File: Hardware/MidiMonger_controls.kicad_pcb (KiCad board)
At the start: 2 copper layers, 40 x 110 mm, 31 parts, among them J10 Gate8_Out, J11 CV1_Out, J12 CV2_Out, J13 CV3_Out, J14 CV4_Out, J15 USB_B_Wurth, J16 MIDI_DIN, J2 Gate3_Out, J20 Conn_01x09_Female, J21 Conn_01x08_Female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

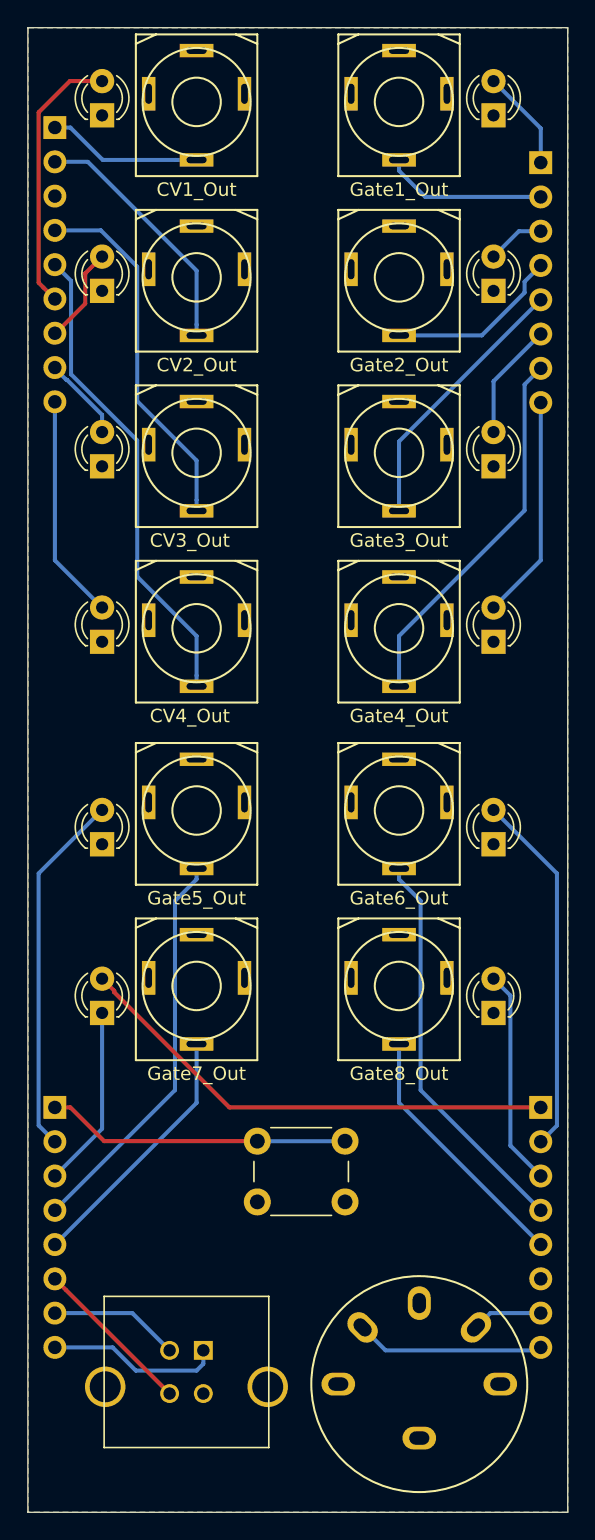
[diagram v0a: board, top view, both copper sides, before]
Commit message: Panel first draft with components
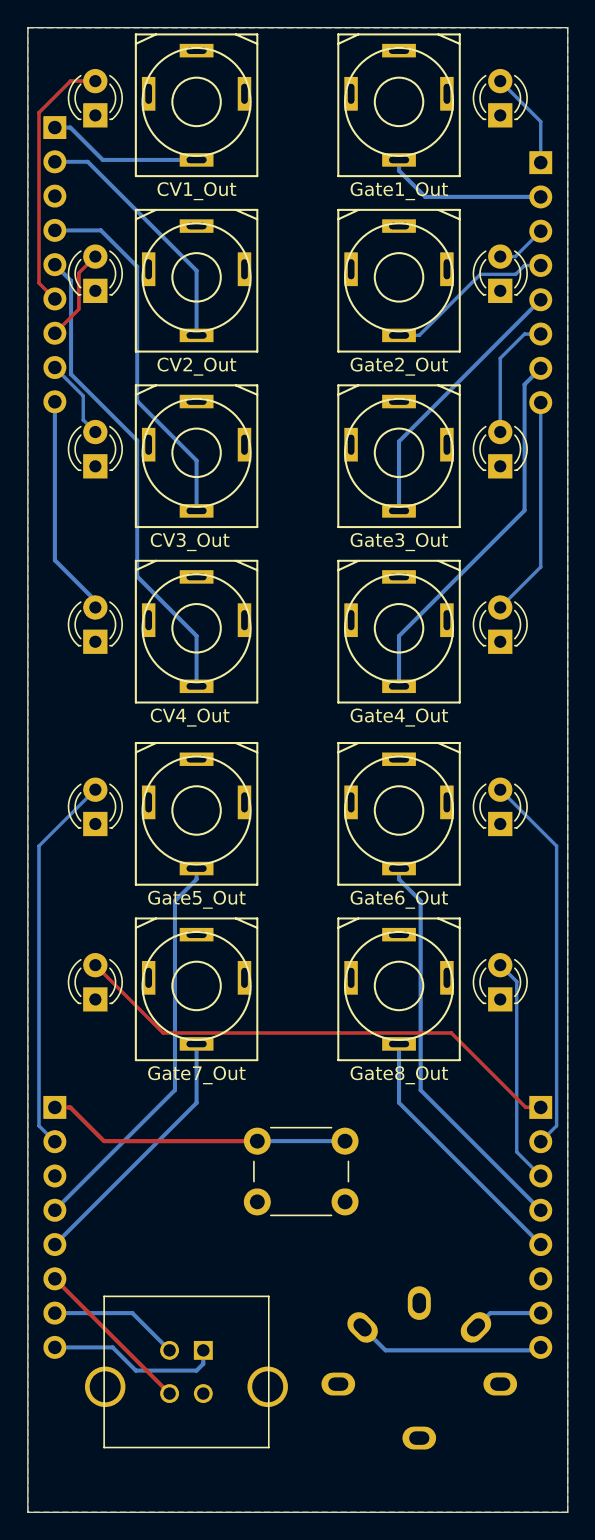
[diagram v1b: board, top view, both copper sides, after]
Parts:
- moved D10 1.58 mm to (131.0, 99.0)
- moved D9 1.58 mm to (101.0, 99.0)
- moved D11 1.12 mm to (101.0, 112.0)
- moved D12 1.12 mm to (131.0, 112.0)
- moved D1 0.50 mm to (131.0, 46.5)
- moved D2 0.50 mm to (131.0, 59.5)
- moved D3 0.50 mm to (131.0, 72.5)
- moved D4 0.50 mm to (131.0, 85.5)
- moved D5 0.50 mm to (101.0, 46.5)
- moved D6 0.50 mm to (101.0, 59.5)
- moved D7 0.50 mm to (101.0, 72.5)
- moved D8 0.50 mm to (101.0, 85.5)
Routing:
- net GND: track 13.5 -> 0.00 mm
- net GATE6_LED_OUT: track 27.0 -> 28.3 mm
- net GATE5_LED_OUT: track 27.0 -> 28.3 mm
- net GATE7_LED_OUT: track 36.5 -> 37.4 mm
- net GATE8_LED_OUT: track 16.1 -> 16.9 mm
- net CV1_LED_OUT: track 20.0 -> 19.4 mm
- net GATE2_LED_OUT: track 4.28 -> 3.78 mm

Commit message: First draft of PCBs completed and sent to JLC
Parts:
- moved J15 2.06 mm to (108.5, 140.0)
- moved SW1 2.02 mm to (112.8, 124.5)
- moved D10 2.00 mm to (131.0, 101.0)
- moved D11 2.00 mm to (101.0, 114.0)
- moved D12 2.00 mm to (131.0, 114.0)
- moved D9 2.00 mm to (101.0, 101.0)
- moved J10 2.00 mm to (123.5, 114.0)
- moved J7 2.00 mm to (108.5, 101.0)
- moved J8 2.00 mm to (123.5, 101.0)
- moved J9 2.00 mm to (108.5, 114.0)
- moved J16 1.00 mm to (125.0, 135.5)
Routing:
- net GATE6_LED_OUT: track 28.3 -> 26.2 mm
- net GATE5_LED_OUT: track 28.3 -> 26.2 mm
- net GATE8_OUT: track 19.2 -> 17.2 mm
- net GATE7_OUT: track 19.2 -> 17.2 mm
- net GATE6_OUT: track 29.7 -> 27.7 mm
- net GATE5_OUT: track 29.7 -> 27.7 mm
- net USB_DP: track 12.0 -> 13.8 mm
- net USB_VBUS: track 13.2 -> 14.2 mm
- net RESET_SWITCH: track 22.5 -> 23.4 mm
- net GATE7_LED_OUT: track 37.4 -> 36.5 mm
- net GATE2_OUT: track 12.6 -> 13.5 mm
- net GATE3_LED_OUT: track 9.21 -> 8.50 mm
- net CV4_LED_OUT: track 16.6 -> 17.2 mm
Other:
- net class Default: clearance 0.2 -> 0.25; trace_width 0.25 -> 0.4
- rule trace_clearance: 0.2 -> 0.25
- board text added: "CV1"
- board text added: "CV1-4LED"
- board text added: "CV2"
- board text added: "CV3"
- board text added: "DM"
- board text added: "G1"
- board text added: "G1L"
- board text added: "G2L"
- board text added: "G3L"
- board text added: "G4"
- board text added: "G4L"
- board text added: "G5"
- board text added: "G5L"
- board text added: "G6"
- board text added: "G6L"
- board text added: "G7"
- board text added: "G7L"
- board text added: "G8"
- board text added: "G8L"
- board text added: "GND"
- board text added: "MD"
- board text added: "MV"
- board text added: "Mountjoy Modular MIDI Monger Controls v1.0"
- board text added: "RES"
- board text added: "USB DP"
- board text added: "VBUS"

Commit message: Fixed grounding error with output jacks on controls board
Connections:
- J10 pad 2: GND -> Net-(J10-Pad2)
- J11 pad 2: GND -> Net-(J11-Pad2)
- J12 pad 2: GND -> Net-(J12-Pad2)
- J13 pad 2: GND -> Net-(J13-Pad2)
- J14 pad 2: GND -> Net-(J14-Pad2)
- J2 pad 2: GND -> Net-(J2-Pad2)
- J3 pad 2: GND -> Net-(J3-Pad2)
- J4 pad 2: GND -> Net-(J4-Pad2)
- J5 pad 2: GND -> Net-(J5-Pad2)
- J7 pad 2: GND -> Net-(J7-Pad2)
- J8 pad 2: GND -> Net-(J8-Pad2)
- J9 pad 2: GND -> Net-(J9-Pad2)
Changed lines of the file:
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@@
-(kicad_pcb (version 20171130) (host pcbnew "(5.1.4)-1")
+(kicad_pcb (version 20171130) (host pcbnew "(5.1.5)-3")
   (general
     (thickness 1.6)
@@
     (zones 0)
     (modules 31)
-    (nets 36)
+    (nets 49)
   )
   (page A4)
   (layers
-    (0 F.Cu signal hide)
-    (31 B.Cu signal hide)
+    (0 F.Cu signal)
+    (31 B.Cu signal)
     (32 B.Adhes user)
     (33 F.Adhes user)
@@
   (net 34 CV3_OUT)
   (net 35 CV4_OUT)
+  (net 36 "Net-(J2-Pad2)")
+  (net 37 "Net-(J3-Pad2)")
+  (net 38 "Net-(J4-Pad2)")
+  (net 39 "Net-(J5-Pad2)")
+  (net 40 "Net-(J7-Pad2)")
+  (net 41 "Net-(J8-Pad2)")
+  (net 42 "Net-(J9-Pad2)")
+  (net 43 "Net-(J10-Pad2)")
+  (net 44 "Net-(J11-Pad2)")
+  (net 45 "Net-(J12-Pad2)")
+  (net 46 "Net-(J13-Pad2)")
+  (net 47 "Net-(J14-Pad2)")
+  (net 48 "Net-(J15-Pad5)")
   (net_class Default "This is the default net class."
     (clearance 0.25)
@@
     (add_net MIDI_DATA)
     (add_net MIDI_VREF)
+    (add_net "Net-(J10-Pad2)")
+    (add_net "Net-(J11-Pad2)")
+    (add_net "Net-(J12-Pad2)")
+    (add_net "Net-(J13-Pad2)")
+    (add_net "Net-(J14-Pad2)")
+    (add_net "Net-(J15-Pad5)")
     (add_net "Net-(J16-Pad1)")
     (add_net "Net-(J16-Pad2)")
     (add_net "Net-(J16-Pad3)")
     (add_net "Net-(J16-Pad6)")
+    (add_net "Net-(J2-Pad2)")
+    (add_net "Net-(J3-Pad2)")
+    (add_net "Net-(J4-Pad2)")
+    (add_net "Net-(J5-Pad2)")
+    (add_net "Net-(J7-Pad2)")
+    (add_net "Net-(J8-Pad2)")
+    (add_net "Net-(J9-Pad2)")
     (add_net RESET_SWITCH)
     (add_net USB_DM)
     (add_net USB_DP)
     (add_net USB_VBUS)
+  )
+  (module Custom_Footprints:USB_B_Wurth (layer F.Cu)
+    (at 108.5 140)
+    (descr "USB B female connector, straight, rugged")
+    (tags "USB_B_MUSB_Straight female connector straight rugged MUSB D511")
+    (fp_text reference J15 (at -0.9 -5) (layer F.SilkS) hide
+      (effects (font (size 1 1) (thickness 0.15)))
+    )
+    (fp_text value USB_B_Wurth (at -0.9 8.7) (layer F.Fab)
+      (effects (font (size 1 1) (thickness 0.15)))
+    )
+    (fp_line (start 4.85 -4) (end 4.85 7.2) (layer F.SilkS) (width 0.12))
+    (fp_line (start -7.35 7.2) (end 4.85 7.2) (layer F.SilkS) (width 0.12))
+    (fp_line (start -7.35 -4) (end 4.85 -4) (layer F.SilkS) (width 0.12))
+    (fp_line (start -7.35 -4) (end -7.35 7.2) (layer F.SilkS) (width 0.12))
+    (fp_line (start -9 -4.3) (end 6.5 -4.3) (layer F.CrtYd) (width 0.05))
+    (fp_line (start 6.5 -4.3) (end 6.5 7.5) (layer F.CrtYd) (width 0.05))
+    (fp_line (start 6.5 7.5) (end -9 7.5) (layer F.CrtYd) (width 0.05))
+    (fp_line (start -9 7.5) (end -9 -4.3) (layer F.CrtYd) (width 0.05))
+    (pad 5 thru_hole circle (at 4.77 2.7) (size 3 3) (drill 2.3) (layers *.Cu *.Mask)
+      (net 48 "Net-(J15-Pad5)"))
+    (pad 4 thru_hole circle (at 0 3.2) (size 1.4 1.4) (drill 0.92) (layers *.Cu *.Mask)
+      (net 2 GND))
+    (pad 3 thru_hole circle (at -2.5 3.2) (size 1.4 1.4) (drill 0.92) (layers *.Cu *.Mask)
+      (net 26 USB_DP))
+    (pad 1 thru_hole rect (at 0 0) (size 1.4 1.4) (drill 0.92) (layers *.Cu *.Mask)
+      (net 27 USB_VBUS))
+    (pad "" thru_hole circle (at -7.27 2.7) (size 3 3) (drill 2.3) (layers *.Cu *.Mask))
+    (pad 2 thru_hole circle (at -2.5 0) (size 1.4 1.4) (drill 0.92) (layers *.Cu *.Mask)
+      (net 25 USB_DM))
   )
   (module Custom_Footprints:MIDI_DIN (layer F.Cu)
@@
     )
   )
-  (module Custom_Footprints:USB_B_Wurth (layer F.Cu)
-    (at 108.5 140)
-    (descr "USB B female connector, straight, rugged")
-    (tags "USB_B_MUSB_Straight female connector straight rugged MUSB D511")
-    (fp_text reference J15 (at -0.9 -5) (layer F.SilkS) hide
-      (effects (font (size 1 1) (thickness 0.15)))
-    )
-    (fp_text value USB_B_Wurth (at -0.9 8.7) (layer F.Fab)
-      (effects (font (size 1 1) (thickness 0.15)))
-    )
-    (fp_line (start 4.85 -4) (end 4.85 7.2) (layer F.SilkS) (width 0.12))
-    (fp_line (start -7.35 7.2) (end 4.85 7.2) (layer F.SilkS) (width 0.12))
-    (fp_line (start -7.35 -4) (end 4.85 -4) (layer F.SilkS) (width 0.12))
-    (fp_line (start -7.35 -4) (end -7.35 7.2) (layer F.SilkS) (width 0.12))
-    (fp_line (start -9 -4.3) (end 6.5 -4.3) (layer F.CrtYd) (width 0.05))
-    (fp_line (start 6.5 -4.3) (end 6.5 7.5) (layer F.CrtYd) (width 0.05))
-    (fp_line (start 6.5 7.5) (end -9 7.5) (layer F.CrtYd) (width 0.05))
-    (fp_line (start -9 7.5) (end -9 -4.3) (layer F.CrtYd) (width 0.05))
-    (pad "" thru_hole circle (at 4.77 2.7) (size 3 3) (drill 2.3) (layers *.Cu *.Mask))
-    (pad 4 thru_hole circle (at 0 3.2) (size 1.4 1.4) (drill 0.92) (layers *.Cu *.Mask)
-      (net 2 GND))
-    (pad 3 thru_hole circle (at -2.5 3.2) (size 1.4 1.4) (drill 0.92) (layers *.Cu *.Mask)
-      (net 26 USB_DP))
-    (pad 1 thru_hole rect (at 0 0) (size 1.4 1.4) (drill 0.92) (layers *.Cu *.Mask)
-      (net 27 USB_VBUS))
-    (pad "" thru_hole circle (at -7.27 2.7) (size 3 3) (drill 2.3) (layers *.Cu *.Mask))
-    (pad 2 thru_hole circle (at -2.5 0) (size 1.4 1.4) (drill 0.92) (layers *.Cu *.Mask)
-      (net 25 USB_DM))
-  )
   (module Custom_Footprints:Cliff_3.5mm_Stereo_Jack (layer F.Cu)
     (at 123.5 72.5)
@@
       (net 2 GND))
     (pad 2 thru_hole rect (at -3.55 -1.6 90) (size 2.5 1) (drill oval 1.5 0.5) (layers *.Cu *.Mask F.SilkS)
-      (net 2 GND))
+      (net 36 "Net-(J2-Pad2)"))
     (pad 3 thru_hole rect (at 0 3.3) (size 2.5 1) (drill oval 1.5 0.5) (layers *.Cu *.Mask F.SilkS)
       (net 23 GATE3_OUT))
@@
       (net 2 GND))
     (pad 2 thru_hole rect (at -3.55 -1.6 90) (size 2.5 1) (drill oval 1.5 0.5) (layers *.Cu *.Mask F.SilkS)
-      (net 2 GND))
+      (net 37 "Net-(J3-Pad2)"))
     (pad 3 thru_hole rect (at 0 3.3) (size 2.5 1) (drill oval 1.5 0.5) (layers *.Cu *.Mask F.SilkS)
       (net 24 GATE4_OUT))
@@
       (net 2 GND))
     (pad 2 thru_hole rect (at -3.55 -1.6 90) (size 2.5 1) (drill oval 1.5 0.5) (layers *.Cu *.Mask F.SilkS)
-      (net 2 GND))
+      (net 38 "Net-(J4-Pad2)"))
     (pad 3 thru_hole rect (at 0 3.3) (size 2.5 1) (drill oval 1.5 0.5) (layers *.Cu *.Mask F.SilkS)
       (net 21 GATE1_OUT))
@@
       (net 2 GND))
     (pad 2 thru_hole rect (at -3.55 -1.6 90) (size 2.5 1) (drill oval 1.5 0.5) (layers *.Cu *.Mask F.SilkS)
-      (net 2 GND))
+      (net 39 "Net-(J5-Pad2)"))
     (pad 3 thru_hole rect (at 0 3.3) (size 2.5 1) (drill oval 1.5 0.5) (layers *.Cu *.Mask F.SilkS)
       (net 22 GATE2_OUT))
@@
       (net 2 GND))
     (pad 2 thru_hole rect (at -3.55 -1.6 90) (size 2.5 1) (drill oval 1.5 0.5) (layers *.Cu *.Mask F.SilkS)
-      (net 2 GND))
+      (net 40 "Net-(J7-Pad2)"))
     (pad 3 thru_hole rect (at 0 3.3) (size 2.5 1) (drill oval 1.5 0.5) (layers *.Cu *.Mask F.SilkS)
       (net 20 GATE5_OUT))
@@
       (net 2 GND))
     (pad 2 thru_hole rect (at -3.55 -1.6 90) (size 2.5 1) (drill oval 1.5 0.5) (layers *.Cu *.Mask F.SilkS)
-      (net 2 GND))
+      (net 41 "Net-(J8-Pad2)"))
     (pad 3 thru_hole rect (at 0 3.3) (size 2.5 1) (drill oval 1.5 0.5) (layers *.Cu *.Mask F.SilkS)
       (net 19 GATE6_OUT))
@@
       (net 2 GND))
     (pad 2 thru_hole rect (at -3.55 -1.6 90) (size 2.5 1) (drill oval 1.5 0.5) (layers *.Cu *.Mask F.SilkS)
-      (net 2 GND))
+      (net 42 "Net-(J9-Pad2)"))
     (pad 3 thru_hole rect (at 0 3.3) (size 2.5 1) (drill oval 1.5 0.5) (layers *.Cu *.Mask F.SilkS)
       (net 18 GATE7_OUT))
@@
       (net 2 GND))
     (pad 2 thru_hole rect (at -3.55 -1.6 90) (size 2.5 1) (drill oval 1.5 0.5) (layers *.Cu *.Mask F.SilkS)
-      (net 2 GND))
+      (net 43 "Net-(J10-Pad2)"))
     (pad 3 thru_hole rect (at 0 3.3) (size 2.5 1) (drill oval 1.5 0.5) (layers *.Cu *.Mask F.SilkS)
       (net 17 GATE8_OUT))
@@
       (net 2 GND))
     (pad 2 thru_hole rect (at -3.55 -1.6 90) (size 2.5 1) (drill oval 1.5 0.5) (layers *.Cu *.Mask F.SilkS)
-      (net 2 GND))
+      (net 44 "Net-(J11-Pad2)"))
     (pad 3 thru_hole rect (at 0 3.3) (size 2.5 1) (drill oval 1.5 0.5) (layers *.Cu *.Mask F.SilkS)
       (net 32 CV1_OUT))
@@
       (net 2 GND))
     (pad 2 thru_hole rect (at -3.55 -1.6 90) (size 2.5 1) (drill oval 1.5 0.5) (layers *.Cu *.Mask F.SilkS)
-      (net 2 GND))
+      (net 45 "Net-(J12-Pad2)"))
     (pad 3 thru_hole rect (at 0 3.3) (size 2.5 1) (drill oval 1.5 0.5) (layers *.Cu *.Mask F.SilkS)
       (net 33 CV2_OUT))
@@
       (net 2 GND))
     (pad 2 thru_hole rect (at -3.55 -1.6 90) (size 2.5 1) (drill oval 1.5 0.5) (layers *.Cu *.Mask F.SilkS)
-      (net 2 GND))
+      (net 46 "Net-(J13-Pad2)"))
     (pad 3 thru_hole rect (at 0 3.3) (size 2.5 1) (drill oval 1.5 0.5) (layers *.Cu *.Mask F.SilkS)
       (net 34 CV3_OUT))
@@
       (net 2 GND))
     (pad 2 thru_hole rect (at -3.55 -1.6 90) (size 2.5 1) (drill oval 1.5 0.5) (layers *.Cu *.Mask F.SilkS)
-      (net 2 GND))
+      (net 47 "Net-(J14-Pad2)"))
     (pad 3 thru_hole rect (at 0 3.3) (size 2.5 1) (drill oval 1.5 0.5) (layers *.Cu *.Mask F.SilkS)
       (net 35 CV4_OUT))
